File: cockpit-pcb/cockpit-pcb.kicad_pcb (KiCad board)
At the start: 2 copper layers, 75 x 55 mm, 41 parts, among them J1 Network Connector, J2 B2B STLink connector, SW1 SW_Push, U1 LD39050PU33R, U2 STM32G474RBT6, U3 SN65HVD230, Y1 8MHz

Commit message: Board routing
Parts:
- added J3: Button 1 Connector, Connector_JST:JST_ZH_B2B-ZR_1x02_P1.50mm_Vertical, F.Cu at (258.0, 35.0)
- added J4: Button 2 Connector, Connector_JST:JST_ZH_B2B-ZR_1x02_P1.50mm_Vertical, F.Cu at (249.5, 42.0)
- added J5: Button 3 Connector, Connector_JST:JST_ZH_B2B-ZR_1x02_P1.50mm_Vertical, F.Cu at (258.0, 42.0)
- added J6: LED 1 Connector, Connector_JST:JST_PH_B2B-PH-K_1x02_P2.00mm_Vertical, F.Cu at (246.8, 53.2)
- added J7: LED 2 Connector, Connector_JST:JST_PH_B2B-PH-K_1x02_P2.00mm_Vertical, F.Cu at (256.0, 53.2)
- added J8: LED 3 Connector, Connector_JST:JST_PH_B2B-PH-K_1x02_P2.00mm_Vertical, F.Cu at (251.5, 61.5)
- added R6: 33, Resistor_SMD:R_0603_1608Metric, F.Cu at (243.5, 54.0)
- added R7: 33, Resistor_SMD:R_0603_1608Metric, F.Cu at (252.8, 54.0)
- added R8: 33, Resistor_SMD:R_0603_1608Metric, F.Cu at (248.2, 62.2)
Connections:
- U2 pad 20: unconnected-(U2-PA6-Pad20) -> /LED_3
- U2 pad 21: unconnected-(U2-PA7-Pad21) -> /LED_2
- U2 pad 33: unconnected-(U2-PB11-Pad33) -> /BUTTON_3
- U2 pad 34: unconnected-(U2-PB12-Pad34) -> /BUTTON_2
- U2 pad 35: unconnected-(U2-PB13-Pad35) -> /BUTTON_1
- U2 pad 42: unconnected-(U2-PA8-Pad42) -> /LED_1
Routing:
- net /BUTTON_1: track 0.00 -> 44.1 mm, vias 0 -> 1
- net /BUTTON_3: track 0.00 -> 39.4 mm, vias 0 -> 1
- net /BUTTON_2: track 0.00 -> 32.6 mm, vias 0 -> 1
- net /LED_1: track 0.00 -> 32.5 mm, vias 0 -> 2
- net /LED_2: track 0.00 -> 31.4 mm, vias 0 -> 2
- net /LED_3: track 0.00 -> 28.2 mm, vias 0 -> 2
- net Net-(J8-Pin_1): track 0.00 -> 3.28 mm
- net Net-(J7-Pin_1): track 0.00 -> 3.28 mm
- net Net-(J6-Pin_1): track 0.00 -> 3.28 mm
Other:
- board text added: "1"
- board text added: "2"
- board text added: "3"
- board text added: "Buttons"
- board text added: "LEDs"
- board text added: "PA6"
- board text added: "PA7"
- board text added: "PA8"
- board text added: "PB11"
- board text added: "PB12"
- board text added: "PB13"

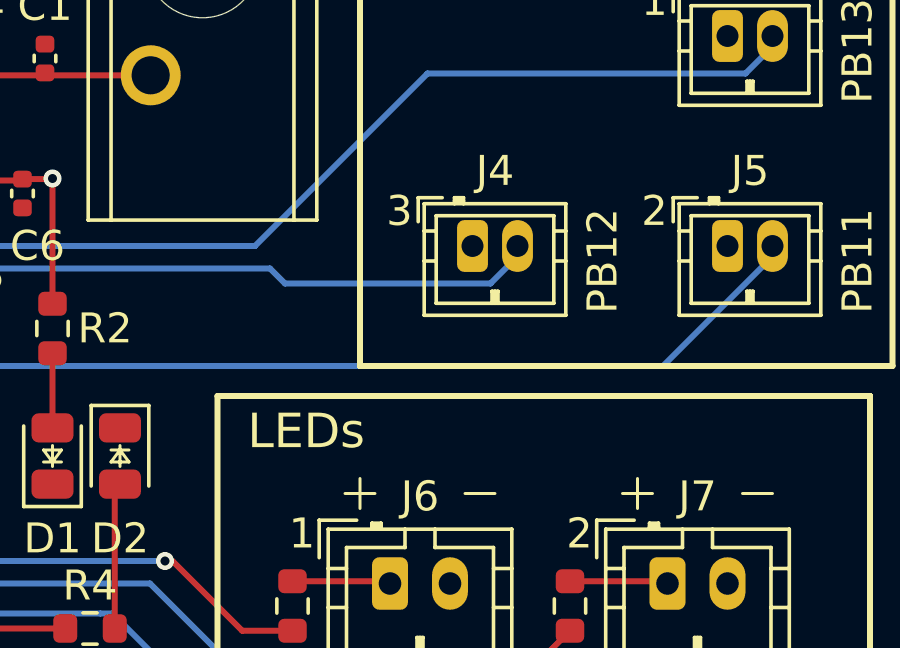
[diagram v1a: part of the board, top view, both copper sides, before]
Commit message: Increase LED resistors
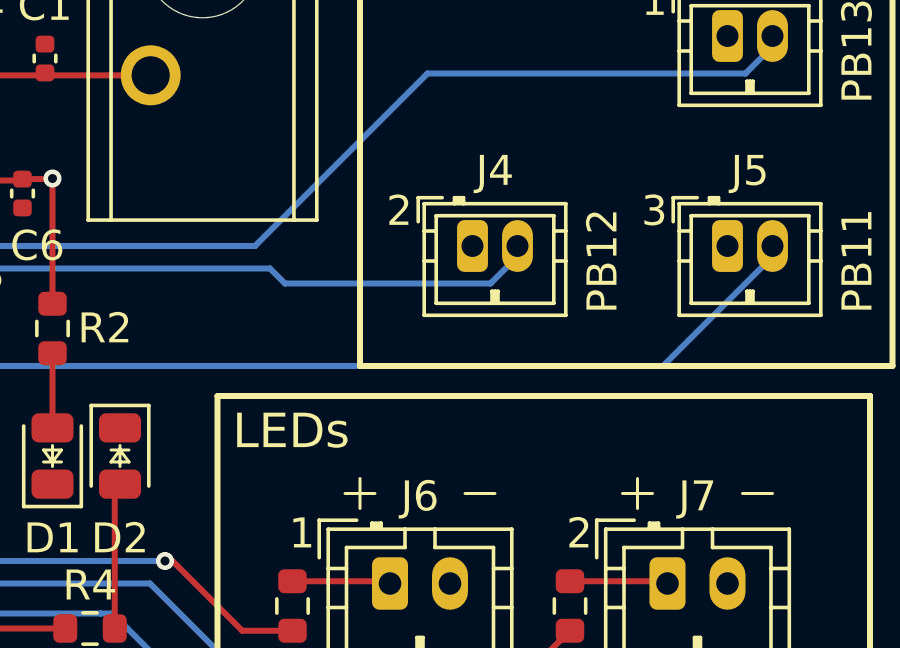
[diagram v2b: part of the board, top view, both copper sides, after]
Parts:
- R2: value 33 -> 510
- R4: value 75 -> 510
- R6, R7, R8: value 33 -> 200
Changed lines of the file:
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@@
 			)
 		)
-		(property "Value" "33"
+		(property "Value" "200"
 			(at 0 1.43 90)
 			(layer "F.Fab")
@@
 			)
 		)
-		(property "JLCPCB" "C23140"
+		(property "JLCPCB" "C8218"
 			(at 0 0 90)
 			(unlocked yes)
@@
 			)
 		)
-		(property "Value" "33"
+		(property "Value" "510"
 			(at 0 1.43 90)
 			(layer "F.Fab")
@@
 			)
 		)
-		(property "JLCPCB" "C23140"
+		(property "JLCPCB" "C23193"
 			(at 0 0 270)
 			(unlocked yes)
@@
 			)
 		)
-		(property "Value" "33"
+		(property "Value" "200"
 			(at 0 1.43 90)
 			(layer "F.Fab")
@@
 			)
 		)
-		(property "JLCPCB" "C23140"
+		(property "JLCPCB" "C8218"
 			(at 0 0 90)
 			(unlocked yes)
@@
 			)
 		)
-		(property "Value" "33"
+		(property "Value" "200"
 			(at 0 1.43 90)
 			(layer "F.Fab")
@@
 			)
 		)
-		(property "JLCPCB" "C23140"
+		(property "JLCPCB" "C8218"
 			(at 0 0 90)
 			(unlocked yes)
@@
 			)
 		)
-		(property "Value" "75"
+		(property "Value" "510"
 			(at 0 1.43 0)
 			(layer "F.Fab")
@@
 			)
 		)
-		(property "JLCPCB" "C4275"
+		(property "JLCPCB" "C23193"
 			(at 0 0 0)
 			(unlocked yes)
@@
 	)
 	(gr_text "3"
-		(at 247.5 40.25 0)
+		(at 256 40.25 0)
 		(layer "F.SilkS" knockout)
 		(effects
@@
 	)
 	(gr_text "LEDs"
-		(at 242 47.5 0)
+		(at 241.5 47.5 0)
 		(layer "F.SilkS")
 		(effects
@@
 	)
 	(gr_text "2"
-		(at 256 40.25 0)
+		(at 247.5 40.25 0)
 		(layer "F.SilkS" knockout)
 		(effects
